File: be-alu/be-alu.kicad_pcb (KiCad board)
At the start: 2 copper layers, 48 x 38 mm, 27 parts, among them J1 Conn_01x02, J2 Conn_01x08, J3 Conn_01x04, J4 Conn_01x08, J5 Conn_01x08, U1 74LS86, U2 74LS86, U3 74LS283, U4 74LS283, U5 74LS245

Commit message: labels and other tweaks on be-alu
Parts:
- moved R1 0.41 mm to (163.2, 49.1)
- moved D1 0.40 mm to (163.2, 43.6)
- moved R8 0.36 mm to (138.0, 48.9)
- moved D8 0.32 mm to (138.0, 43.5)
- moved R7 0.30 mm to (141.6, 48.9)
- moved D2 0.30 mm to (159.6, 43.6)
- moved R2 0.30 mm to (159.6, 49.1)
- moved D7 0.22 mm to (141.6, 43.5)
- moved R6 0.22 mm to (145.2, 48.9)
- moved D3 0.20 mm to (156.0, 43.6)
- moved R3 0.20 mm to (156.0, 49.1)
- moved D6 0.14 mm to (145.2, 43.5)
- moved D5 0.12 mm to (148.8, 43.5)
- moved D4 0.10 mm to (152.4, 43.6)
- moved R4 0.10 mm to (152.4, 49.1)
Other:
- board text added: "1"
- board text added: "128"
- board text added: "16"
- board text added: "2"
- board text added: "32"
- board text added: "4"
- board text added: "64"
- board text added: "8"
- board text added: "BUS"
- board text added: "CLK SU ~OE CO"
- board text added: "LSB"
- board text added: "MSB"
- board text added: "REG A"
- board text added: "REG B"
- board text added: "VCC GND"
- board text added: "be-alu v0.1"

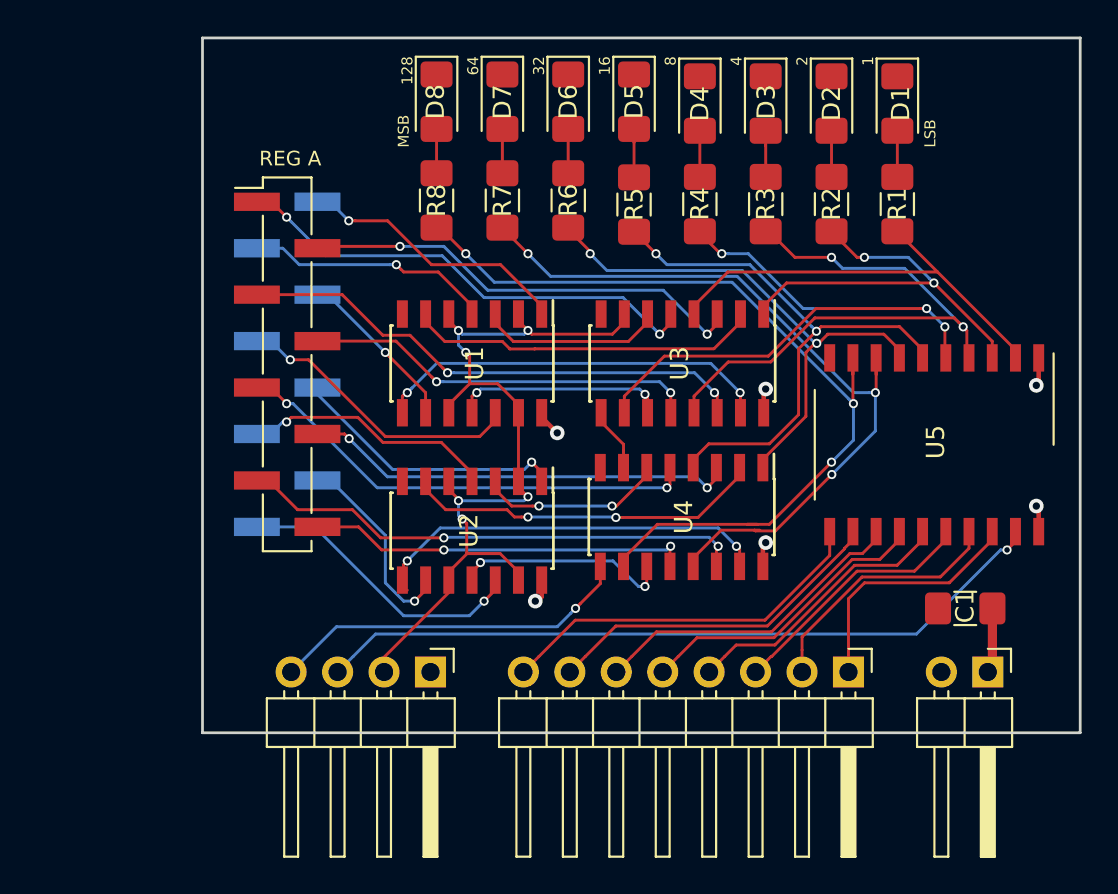
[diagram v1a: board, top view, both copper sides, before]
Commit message: finishing up the first version of be-alu (probably can be ordered as-is after the first batch of be-register is made)
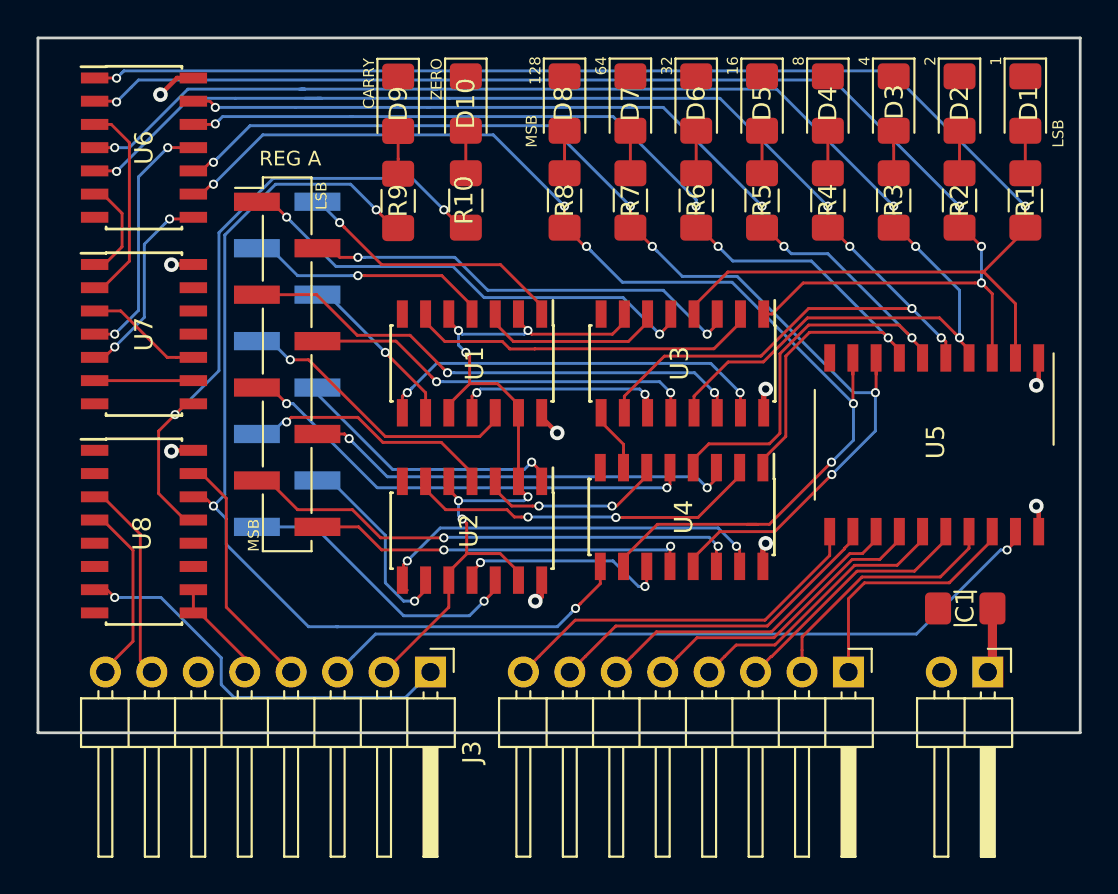
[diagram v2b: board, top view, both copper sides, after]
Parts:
- added D10: LED, LED_SMD:LED_1206_3216Metric_Pad1.42x1.75mm_HandSolder, F.Cu at (139.6, 43.6)
- added D9: LED, LED_SMD:LED_1206_3216Metric_Pad1.42x1.75mm_HandSolder, F.Cu at (135.9, 43.6)
- added R10: 220, Resistor_SMD:R_1206_3216Metric_Pad1.42x1.75mm_HandSolder, F.Cu at (139.6, 48.9)
- added R9: 220, Resistor_SMD:R_1206_3216Metric_Pad1.42x1.75mm_HandSolder, F.Cu at (135.9, 48.9)
- added REF**: OSHW-Logo_5.7x6mm_SilkScreen, Symbol:OSHW-Logo_5.7x6mm_SilkScreen, B.Cu at (168.7, 62.0)
- added U6: 7402, Package_SO:SOIC-14_3.9x8.7mm_P1.27mm, F.Cu at (122.0, 46.0)
- added U7: 7408, Package_SO:SOIC-14_3.9x8.7mm_P1.27mm, F.Cu at (122.0, 56.2)
- added U8: 74LS173, Package_SO:SOIC-16_3.9x9.9mm_P1.27mm, F.Cu at (122.0, 67.0)
- J3: value Conn_01x04 -> Conn_01x08; footprint Connector_PinHeader_2.54mm:PinHeader_1x04_P2.54mm_Horizontal -> Connector_PinHeader_2.54mm:PinHeader_1x08_P2.54mm_Horizontal
- moved R5 7.00 mm to (155.8, 48.9)
- moved R1 7.00 mm to (170.2, 48.9)
- moved R2 7.00 mm to (166.6, 48.9)
- moved R3 7.00 mm to (163.0, 48.9)
- moved R4 7.00 mm to (159.4, 48.9)
- moved D5 7.00 mm to (155.8, 43.6)
- moved D6 7.00 mm to (152.2, 43.6)
- moved D7 7.00 mm to (148.6, 43.6)
- moved D8 7.00 mm to (145.0, 43.6)
- moved D1 7.00 mm to (170.2, 43.6)
- moved D2 7.00 mm to (166.6, 43.6)
- moved D3 7.00 mm to (163.0, 43.6)
- moved D4 7.00 mm to (159.4, 43.6)
- moved R6 7.00 mm to (152.2, 48.9)
- moved R7 7.00 mm to (148.6, 48.9)
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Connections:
- net /~OE renamed /~EO
- J3 pad 4: /CO -> /RST
- U4 pad 9: /CO -> /RAW_CF
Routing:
- net /RAW0: track 24.6 -> 81.6 mm, vias 0 -> 2
- net /RAW_CF: track 0.00 -> 54.7 mm, vias 0 -> 3
- net /RAW1: track 22.8 -> 72.7 mm, vias 2 -> 4
- net /RAW2: track 32.6 -> 76.5 mm, vias 2 -> 4
- net /RAW3: track 36.8 -> 75.0 mm, vias 3 -> 5
- net /RAW_ZF: track 0.00 -> 35.2 mm, vias 0 -> 2
- net /RAW4: track 31.3 -> 65.1 mm, vias 2 -> 4
- net /RAW5: track 29.7 -> 58.4 mm, vias 2 -> 4
- net /CLK: track 0.00 -> 22.3 mm, vias 0 -> 1
- net /RAW6: track 42.4 -> 63.3 mm, vias 3 -> 5
- net /CO: track 19.9 -> 0.00 mm, vias 1 -> 0
- net /RAW7: track 48.1 -> 65.9 mm, vias 3 -> 5
- net Net-(U6-Pad11): track 0.00 -> 13.9 mm, vias 0 -> 2
- net /RST: track 0.00 -> 13.3 mm
- net Net-(U6-Pad3): track 0.00 -> 11.3 mm
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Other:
- board size 48 x 38 mm -> 57 x 38 mm
- net class VCC added: clearance 0.16, trace_width 0.25, via_dia 0.8, via_drill 0.4
- board text added: "BE-ALU v0.1"
- board text added: "CARRY"
- board text added: "CLK SU ~EO RST ~FI CF ZF"
- board text added: "ZERO"
- board text removed: "CLK SU ~OE CO"
- board text removed: "be-alu v0.1"
